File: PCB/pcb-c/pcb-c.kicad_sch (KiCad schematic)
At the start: 40 parts, among them Q1 BC817, Q13 TPCA8120,L1Q, Q2 TPCA8120,L1Q, Q3 BC817, Q4 BC817, Q5 TPCA8120,L1Q, Q6 BC817, Q7 TPCA8120,L1Q, Q8 BC817, Q9 TPCA8120,L1Q

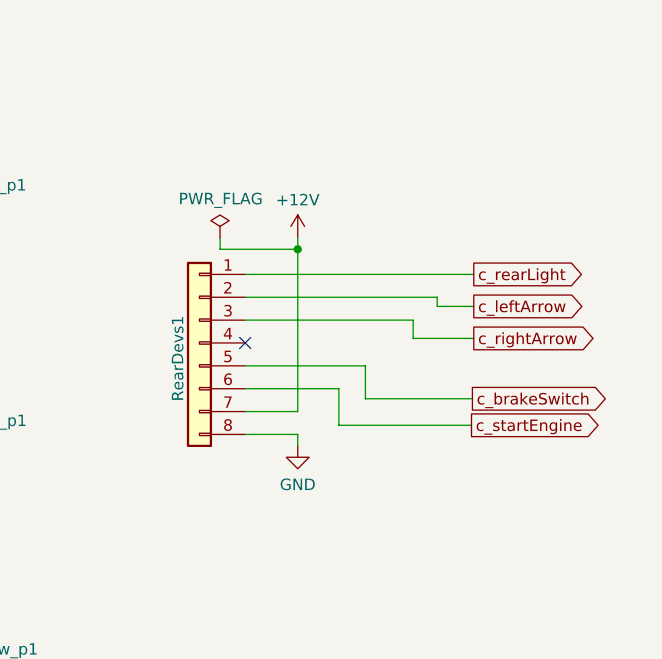
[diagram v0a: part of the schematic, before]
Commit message: Connector pinout configuration change
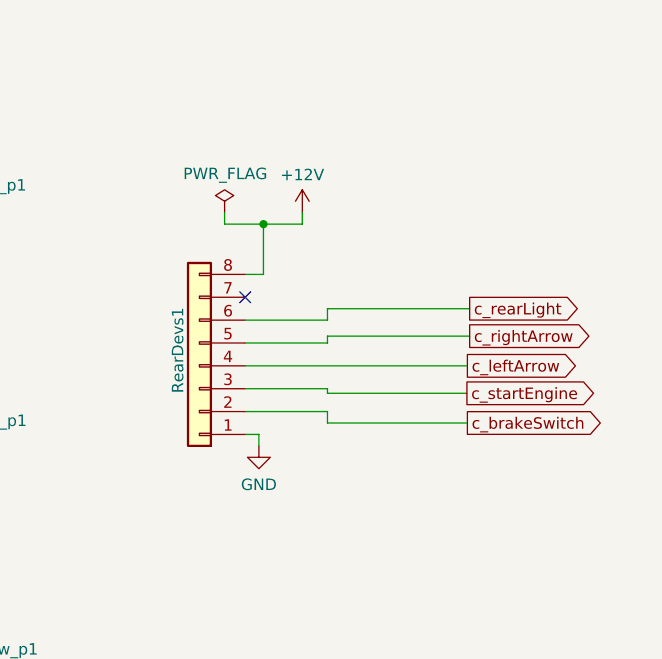
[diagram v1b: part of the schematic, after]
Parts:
- added rightArrow_p1: Conn_01x02, Connector_PinHeader_2.54mm:PinHeader_1x02_P2.54mm_Vertical, symbol Connector_Generic:Conn_01x02
- F1, F2, F3, F4, F5: footprint MSMF050-2:FUSE_F050-2 -> MF-MSMF050-2:FUSE_F050-2
- renumbered rightArrow_p1 to rearLight_p1
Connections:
- net +12V: now also RearDevs1.8 (Pin_8); no longer RearDevs1.7 (Pin_7)
- net GND: now also RearDevs1.1 (Pin_1), rightArrow_p1.1 (Pin_1); no longer RearDevs1.8 (Pin_8)
- net c_brakeSwitch: now also RearDevs1.2 (Pin_2); no longer RearDevs1.5 (Pin_5)
- net c_leftArrow: now also RearDevs1.4 (Pin_4); no longer RearDevs1.2 (Pin_2)
- net c_rearLight: now also RearDevs1.6 (Pin_6); no longer RearDevs1.1 (Pin_1)
- net c_rightArrow: now also RearDevs1.5 (Pin_5); no longer RearDevs1.3 (Pin_3)
- net c_startEngine: now also RearDevs1.3 (Pin_3); no longer RearDevs1.6 (Pin_6)
- net at Q9.5 (D_1), Q9.6 (D_2), Q9.7 (D_3)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: now also rightArrow_p1.2 (Pin_2); no longer rearLight_p1.2 (Pin_2)
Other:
- moved on the sheet: RearDevs1

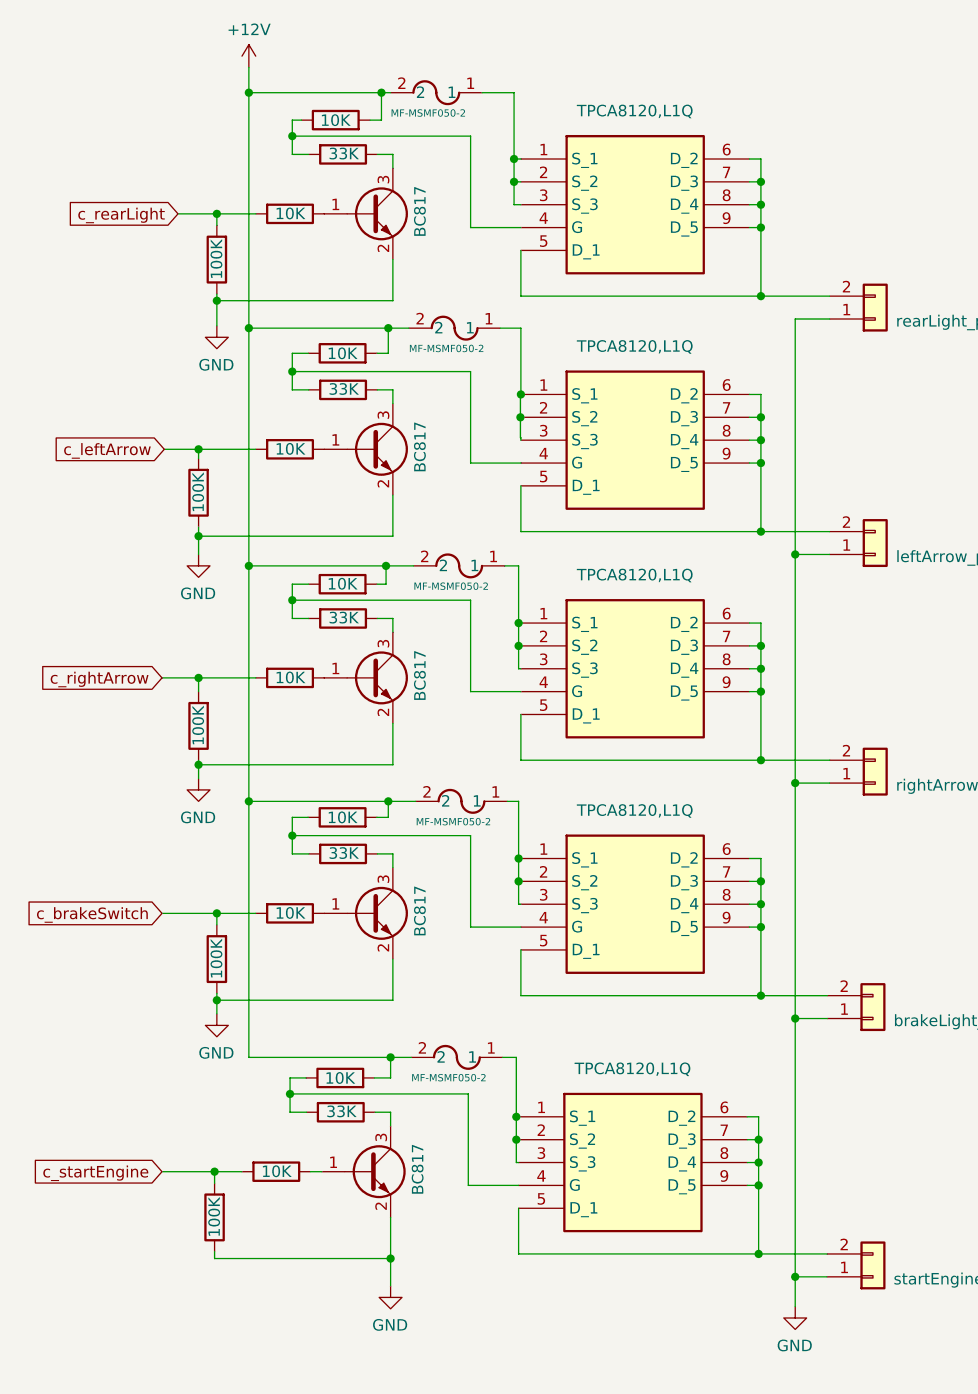
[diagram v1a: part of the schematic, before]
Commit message: Rimozione resistenge sui gates e aggiunta diodo fly-back
PCB size reducing
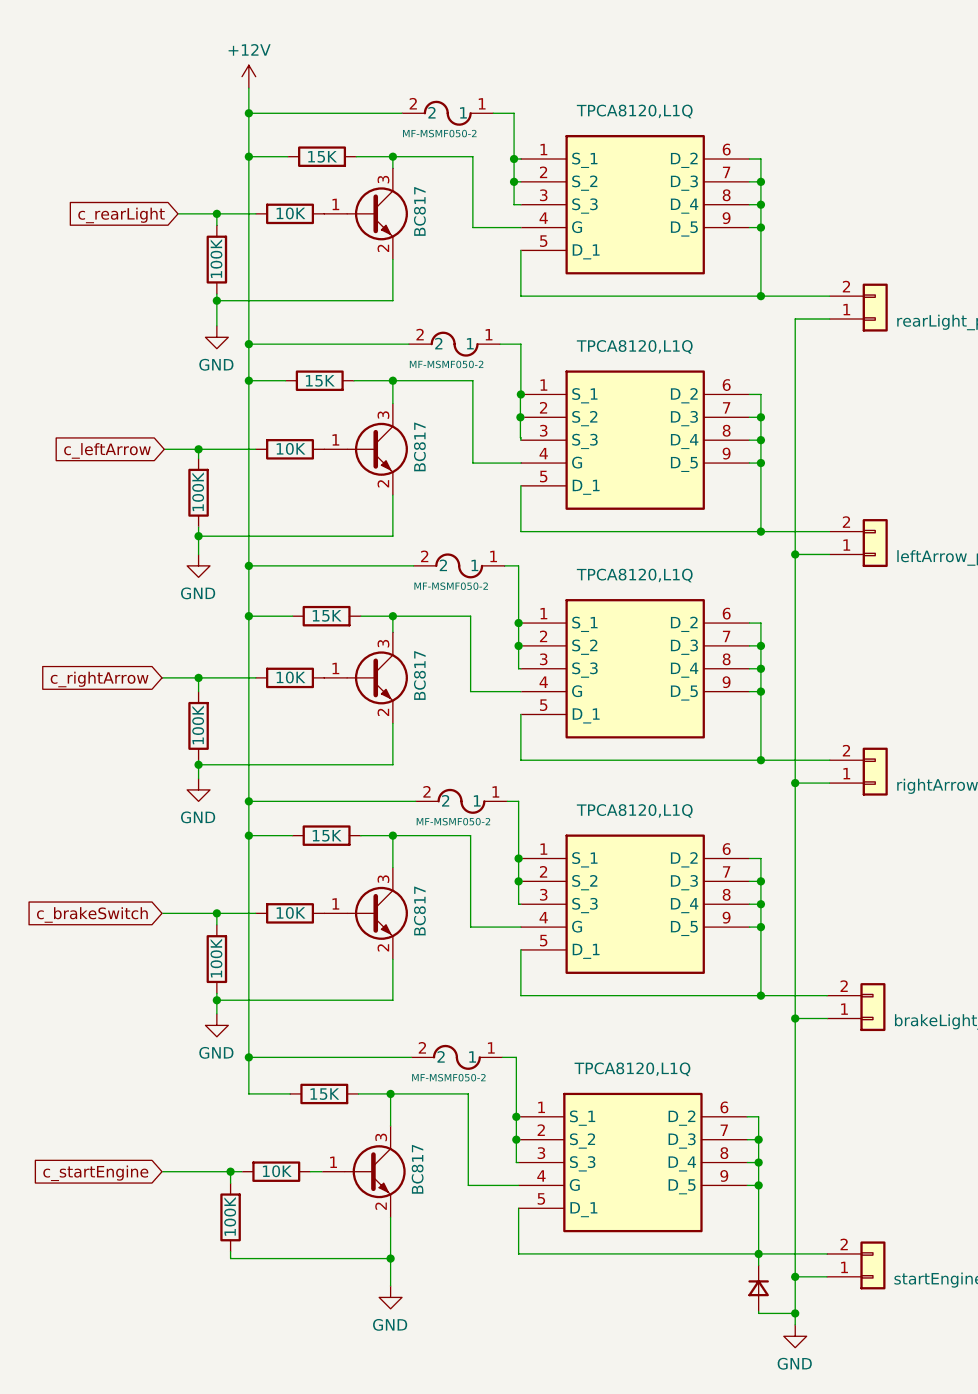
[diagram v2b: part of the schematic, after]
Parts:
- removed R11, R15, R19, R3, R6: 33K, Resistor_SMD:R_1206_3216Metric, symbol Device:R
- added D1: D_Small, Diode_SMD:D_2114_3652Metric_Pad1.85x3.75mm_HandSolder, symbol Device:D_Small
- R10, R14, R18, R2, R5: value 10K -> 15K
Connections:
- net +12V: now also R10.1, R14.1, R18.1, R2.1, R5.1; no longer R10.2, R14.2, R18.2, R2.2, R5.2
- net GND: now also D1.2 (A)
- net at Q4.3 (C): now also Q5.4 (G), R10.2
- net at Q7.4 (G): now also Q6.3 (C), R14.2; no longer R14.1
- net at Q2.4 (G): now also Q1.3 (C), R5.2; no longer R5.1
- net at Q13.4 (G): now also Q3.3 (C), R2.2; no longer R2.1
- net at Q9.4 (G): now also Q8.3 (C), R18.2; no longer R18.1
- net at Q5.5 (D_1), Q5.6 (D_2), Q5.7 (D_3)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: now also D1.1 (K)

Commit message: High current on 2.54 pin-header connector pin 8 fixed
- All electric currect flowed trough the pin 8. Every pin should allows 2A max, so it could be morked in critical area.
  So, due to I am paranoide, I connected the unused pin 7 to the 8.
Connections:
- net +12V: now also RearDevs1.7 (Pin_7)
- no-connect marks 1 -> 0
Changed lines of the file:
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@@
+	)
+	(junction
+		(at 182.372 78.994)
+		(diameter 0)
+		(color 0 0 0 0)
 	)
 	(junction
@@
 		(color 0 0 0 0)
 	)
-	(no_connect
-		(at 180.34 81.534)
-	)
 	(wire
 		(pts
@@
 	(wire
 		(pts
+			(xy 180.34 81.534) (xy 182.372 81.534)
+		)
+		(stroke
+			(width 0)
+			(type default)
+		)
+	)
+	(wire
+		(pts
 			(xy 67.564 119.888) (xy 67.564 118.364)
 		)
@@
 		)
 		(stroke
+			(width 0)
+			(type default)
+		)
+	)
+	(wire
+		(pts
+			(xy 182.372 81.534) (xy 182.372 78.994)
+		)
+		(stroke

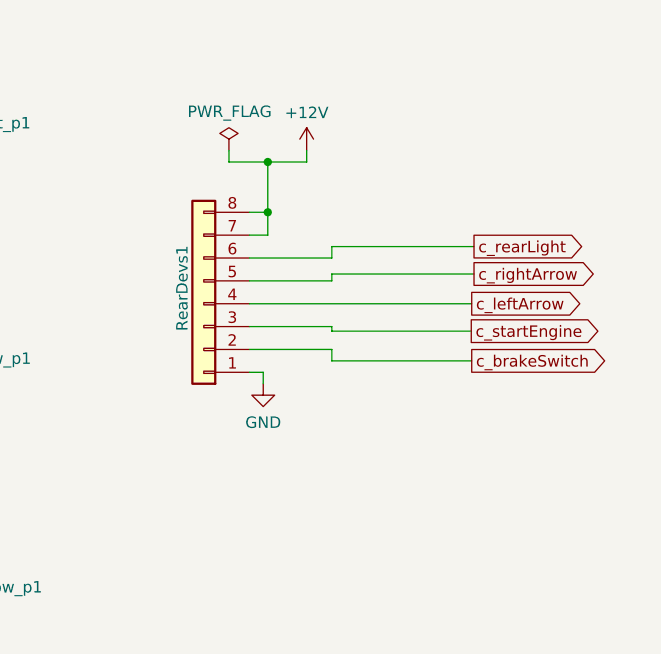
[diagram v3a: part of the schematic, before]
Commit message: RevDev connector has been changed from 8x1 to 5x2 pins
In order to dedicate two pins to GND too, I have used a 10 pins connector
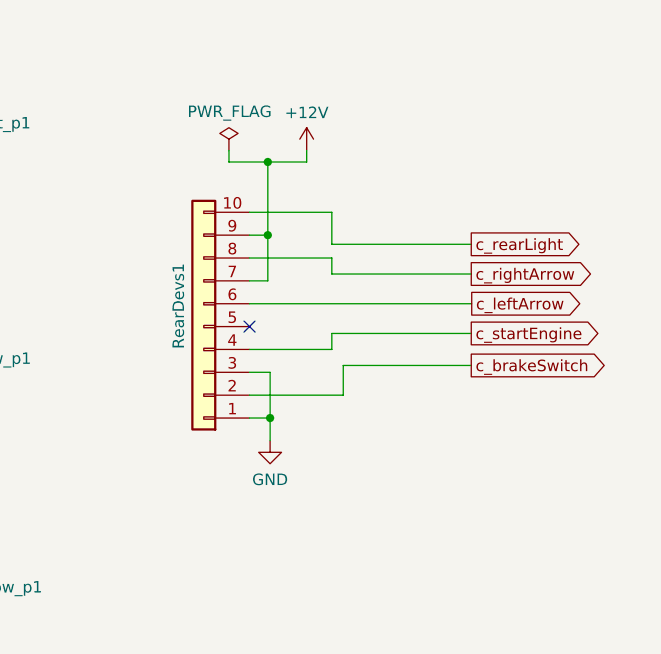
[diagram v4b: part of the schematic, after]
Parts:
- removed RearDevs1: Conn_01x08, Connector_PinHeader_2.54mm:PinHeader_1x08_P2.54mm_Vertical, symbol Connector_Generic:Conn_01x08
- added RearDevs1: Conn_01x10, Connector_PinHeader_2.54mm:PinHeader_2x05_P2.54mm_Vertical, symbol Connector_Generic:Conn_01x10
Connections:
- net +12V: now also RearDevs1.7 (Pin_7), RearDevs1.9 (Pin_9)
- net GND: now also RearDevs1.1 (Pin_1), RearDevs1.3 (Pin_3)
- net c_brakeSwitch: now also RearDevs1.2 (Pin_2)
- net c_leftArrow: now also RearDevs1.6 (Pin_6)
- net c_rearLight: now also RearDevs1.10 (Pin_10)
- net c_rightArrow: now also RearDevs1.8 (Pin_8)
- net c_startEngine: now also RearDevs1.4 (Pin_4)
- no-connect marks 0 -> 1

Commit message: Fly-back diode's wrong value fixed (it is just a notation)
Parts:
- D1: value D_Small -> M7
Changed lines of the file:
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@@
 			)
 		)
-		(property "Value" "D_Small"
+		(property "Value" "M7"
 			(at 132.588 177.7999 90)
 			(effects

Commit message: Mesge from ESP32__dualPCB
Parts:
- added R11, R15, R19, R3, R6: 100K, Resistor_SMD:R_1206_3216Metric, symbol Device:R
- R13, R17, R4, R7, R9: value 10K -> 15K
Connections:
- net +12V: now also R11.1, R15.1, R19.1, R3.1, R6.1
- net at F3.1, Q13.1 (S_1), Q13.2 (S_2)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: now also R19.2
- net at F5.1, Q5.1 (S_1), Q5.2 (S_2)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: now also R3.2
- net at F4.1, Q7.1 (S_1), Q7.2 (S_2)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: now also R15.2
- net at F2.1, Q2.1 (S_1), Q2.2 (S_2)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: now also R6.2
- net at F1.1, Q9.1 (S_1), Q9.2 (S_2)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: now also R11.2
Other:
- moved on the sheet: RearDevs1, brakeLight_p1, leftArrow_p1, rearLight_p1, rightArrow_p1, startEngine_p1
